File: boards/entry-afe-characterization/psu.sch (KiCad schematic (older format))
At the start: 76 parts, among them J10 CONN_3_PWROUT, Q2 2SA2039-TL-E, U10 LT3042, U11 LT3042, U12 MCP1501T-25E/RW, U13 LT3093, U14 PTN78000AAZ, U15 LT3093, U16 LT3042, U17 TL431ACDBZR, U8 TPS54227-DRC, U9 LT3042

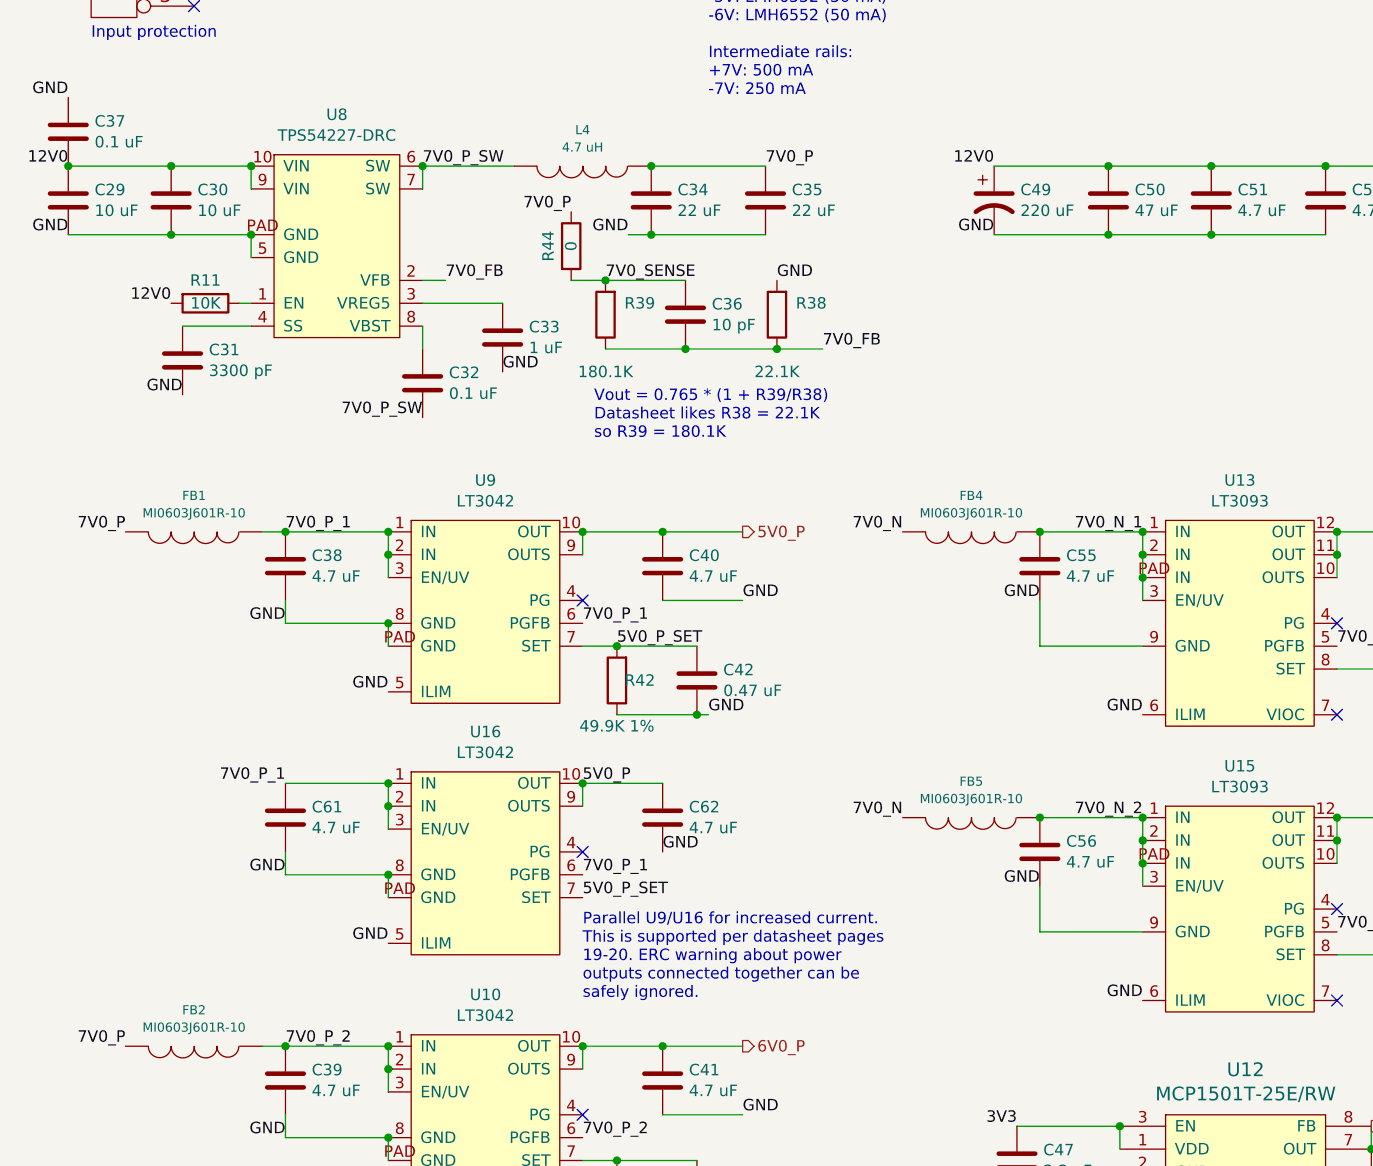
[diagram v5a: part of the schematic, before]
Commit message: Continued design review, added U18 to offset stage
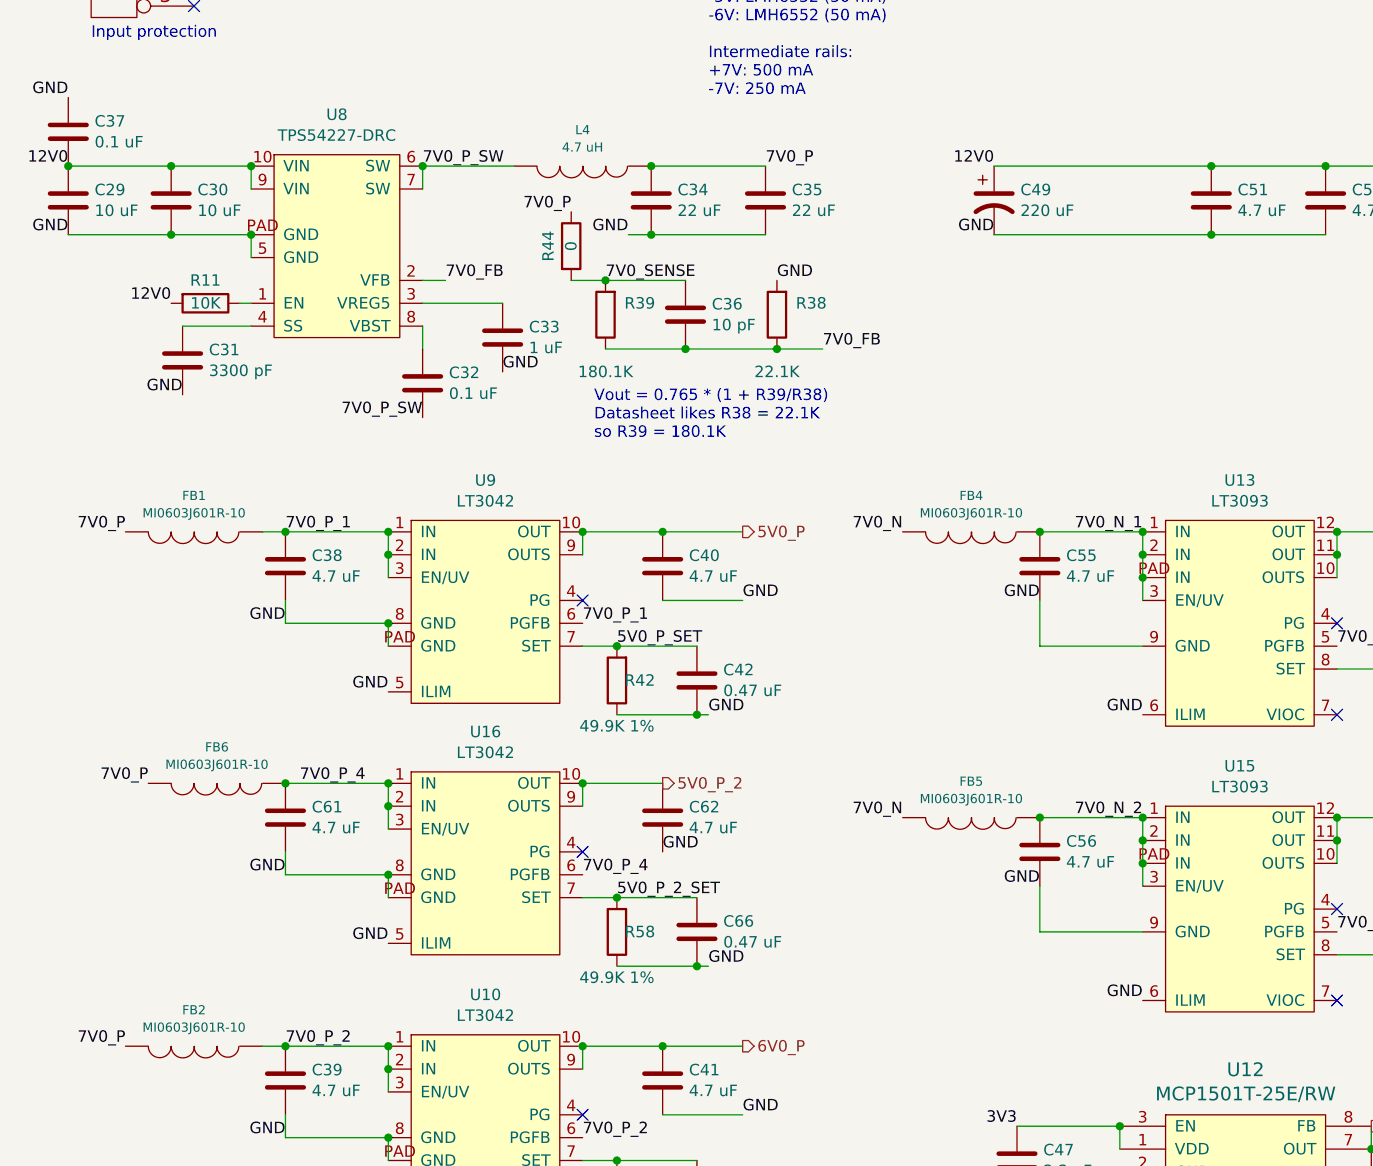
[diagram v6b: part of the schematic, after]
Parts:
- removed C50: 47 uF, symbol device:C
- added C66: 0.47 uF, symbol device:C
- added FB6: MI0603J601R-10, symbol passive-azonenberg:INDUCTOR_PWROUT
- added R58: 49.9K 1%, symbol device:R
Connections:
- net 5V0_P: no longer C62.1, U16.10 (OUT), U16.9 (OUTS)
- net 5V0_P_SET: no longer U16.7 (SET)
- net 7V0_P: now also FB6.2
- net 7V0_P_1: no longer C61.1, U16.1 (IN), U16.2 (IN), U16.3 (EN/UV), U16.6 (PGFB)
- net GND: now also C66.2, R58.1
- new net 5V0_P_2: C62.1, U16.10 (OUT), U16.9 (OUTS)
- new net 5V0_P_2_SET: C66.1, R58.2, U16.7 (SET)
- new net 7V0_P_4: C61.1, FB6.1, U16.1 (IN), U16.2 (IN), U16.3 (EN/UV), U16.6 (PGFB)
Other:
- note removed: "Parallel U9/U16 for increased current.\nThis is supported per datasheet pages\n19-20. ERC warning about power\noutputs connected together can be\nsafely ignored."
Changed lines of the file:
@@
 Sheet 2 8
 Title "Entry-Level Oscilloscope AFE Characterization Platform"
-Date "2020-03-26"
+Date "2020-03-27"
 Rev "0.1"
 Comp "Antikernel Labs"
@@
 Text Label 8200 2000 2    50   ~ 0
 GND
-$Comp
-L device:C C50
-U 1 1 5E865008
-P 5250 1850
-F 0 "C50" H 5365 1896 50  0000 L CNN
-F 1 "47 uF" H 5365 1805 50  0000 L CNN
-F 2 "" H 5288 1700 50  0001 C CNN
-F 3 "" H 5250 1850 50  0001 C CNN
-	1    5250 1850
-	1    0    0    -1
-$EndComp
 Text Label 4750 2000 2    50   ~ 0
 GND
@@
 	1    0    0    -1
 $EndComp
-Wire Wire Line
-	4750 1700 5250 1700
-Wire Wire Line
-	4750 2000 5250 2000
 $Comp
 L device:C C51
@@
 	1    0    0    -1
 $EndComp
-Wire Wire Line
-	5250 1700 5700 1700
-Connection ~ 5250 1700
 Connection ~ 5700 1700
 Wire Wire Line
@@
 Wire Wire Line
 	6200 2000 5700 2000
-Connection ~ 5250 2000
 Connection ~ 5700 2000
-Wire Wire Line
-	5700 2000 5250 2000
 $Comp
 L device:C C55
@@
 Text Label 3100 3800 0    50   ~ 0
 5V0_P_SET
-Text Label 2950 4900 0    50   ~ 0
-5V0_P_SET
-Text Label 2950 4400 0    50   ~ 0
-5V0_P
 Wire Wire Line
 	2950 4500 2950 4400
-Text Label 1650 4400 2    50   ~ 0
-7V0_P_1
+Text Label 2000 4400 2    50   ~ 0
+7V0_P_4
 $Comp
 L device:C C61
@@
 	2100 4500 2100 4600
 Text Label 2950 4800 0    50   ~ 0
-7V0_P_1
+7V0_P_4
 NoConn ~ 2950 4700
 $Comp
@@
 Text Label 3300 4700 0    50   ~ 0
 GND
-Text Notes 2950 5350 0    50   ~ 0
-Parallel U9/U16 for increased current.\nThis is supported per datasheet pages\n19-20. ERC warning about power\noutputs connected together can be\nsafely ignored.
 Text Label 5450 7500 2    50   ~ 0
 5V0_N
@@
 Wire Wire Line
 	1850 800  1950 800
+$Comp
+L device:R R58
+U 1 1 5EA11E7C
+P 3100 5050
+F 0 "R58" H 3000 5050 50  0000 C CNN
+F 1 "49.9K 1%" H 3100 5250 50  0000 C CNN
+F 2 "" V 3030 5050 50  0001 C CNN
+F 3 "" H 3100 5050 50  0001 C CNN
+	1    3100 5050
+	-1   0    0    1
+$EndComp
+Wire Wire Line
+	3100 4900 2950 4900
+Text Label 3500 5200 0    50   ~ 0
+GND
+$Comp
+L device:C C66
+U 1 1 5EA11E88
+P 3450 5050
+F 0 "C66" H 3565 5096 50  0000 L CNN
+F 1 "0.47 uF" H 3565 5005 50  0000 L CNN
+F 2 "" H 3488 4900 50  0001 C CNN
+F 3 "" H 3450 5050 50  0001 C CNN
+	1    3450 5050
+	1    0    0    -1
+$EndComp
+Wire Wire Line
+	3100 5200 3450 5200
+Connection ~ 3450 5200
+Wire Wire Line
+	3450 5200 3500 5200
+Wire Wire Line
+	3450 4900 3100 4900
+Connection ~ 3100 4900
+Text Label 3100 4900 0    50   ~ 0
+5V0_P_2_SET
+Text HLabel 3300 4400 2    50   Output ~ 0
+5V0_P_2
+Text Label 1050 4400 2    50   ~ 0
+7V0_P
+$Comp
+L passive-azonenberg:INDUCTOR_PWROUT FB6
+U 1 1 5EA19602
+P 1350 4400
+F 0 "FB6" V 1192 4400 40  0000 C CNN
+F 1 "MI0603J601R-10" V 1268 4400 40  0000 C CNN
+F 2 "" H 1350 4400 60  0000 C CNN
+F 3 "" H 1350 4400 60  0000 C CNN
+	1    1350 4400
+	0    1    1    0
+$EndComp
+Connection ~ 1650 4400
+Wire Wire Line
+	4750 1700 5700 1700
+Wire Wire Line
+	4750 2000 5700 2000
 $EndSCHEMATC

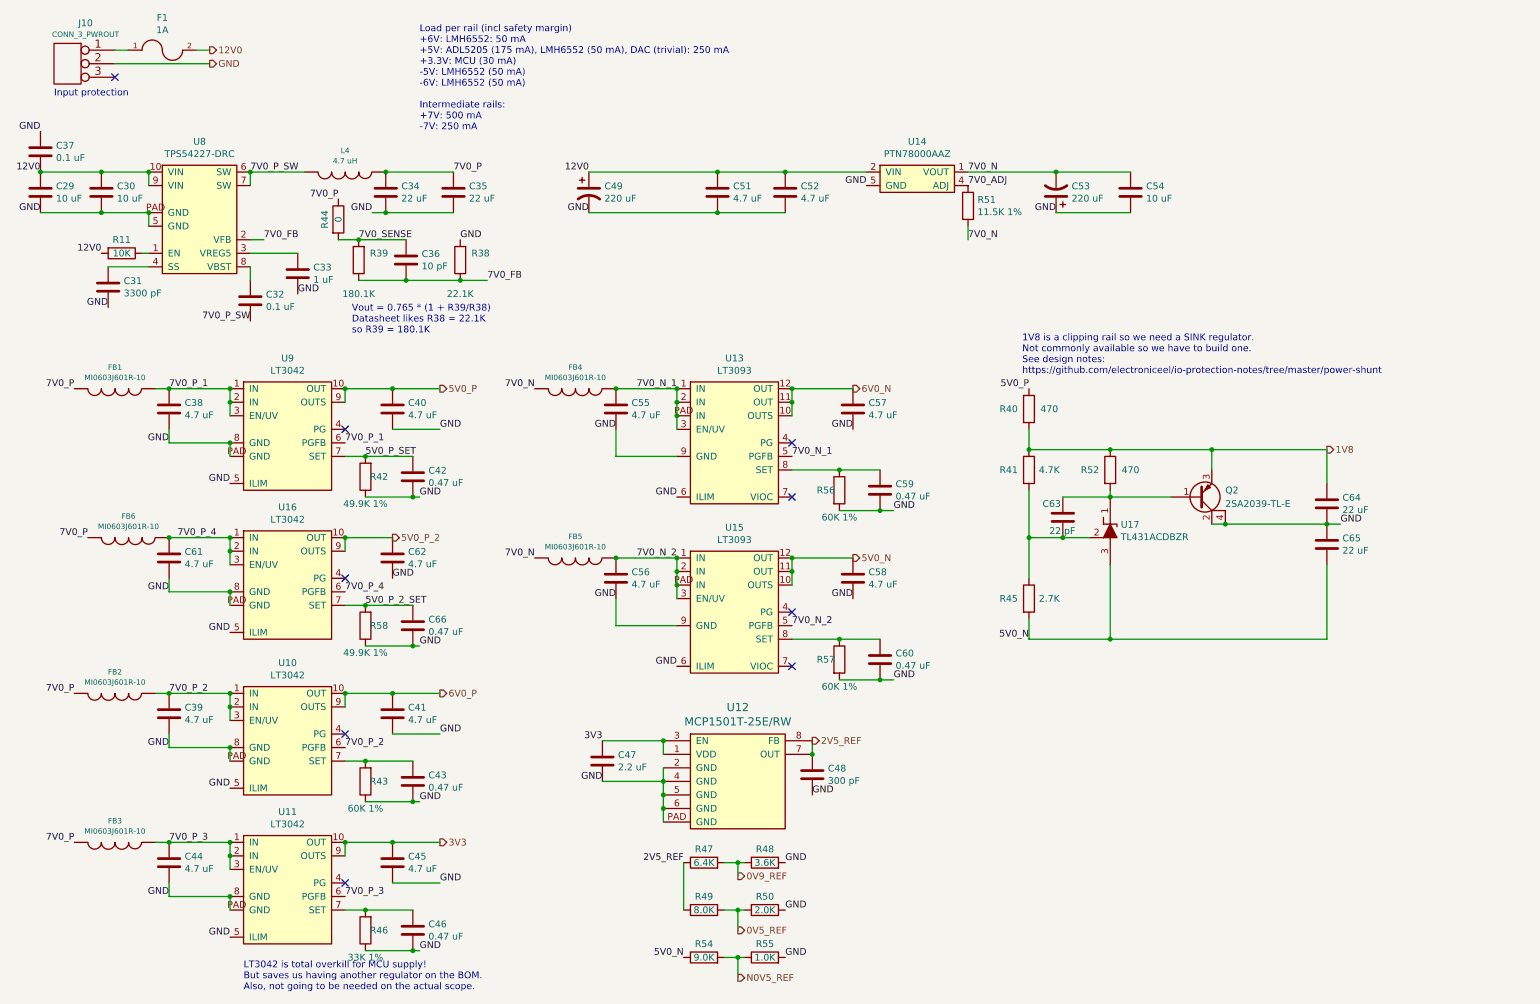
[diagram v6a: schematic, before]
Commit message: Continued design review, began assigning footprints to sch symbols
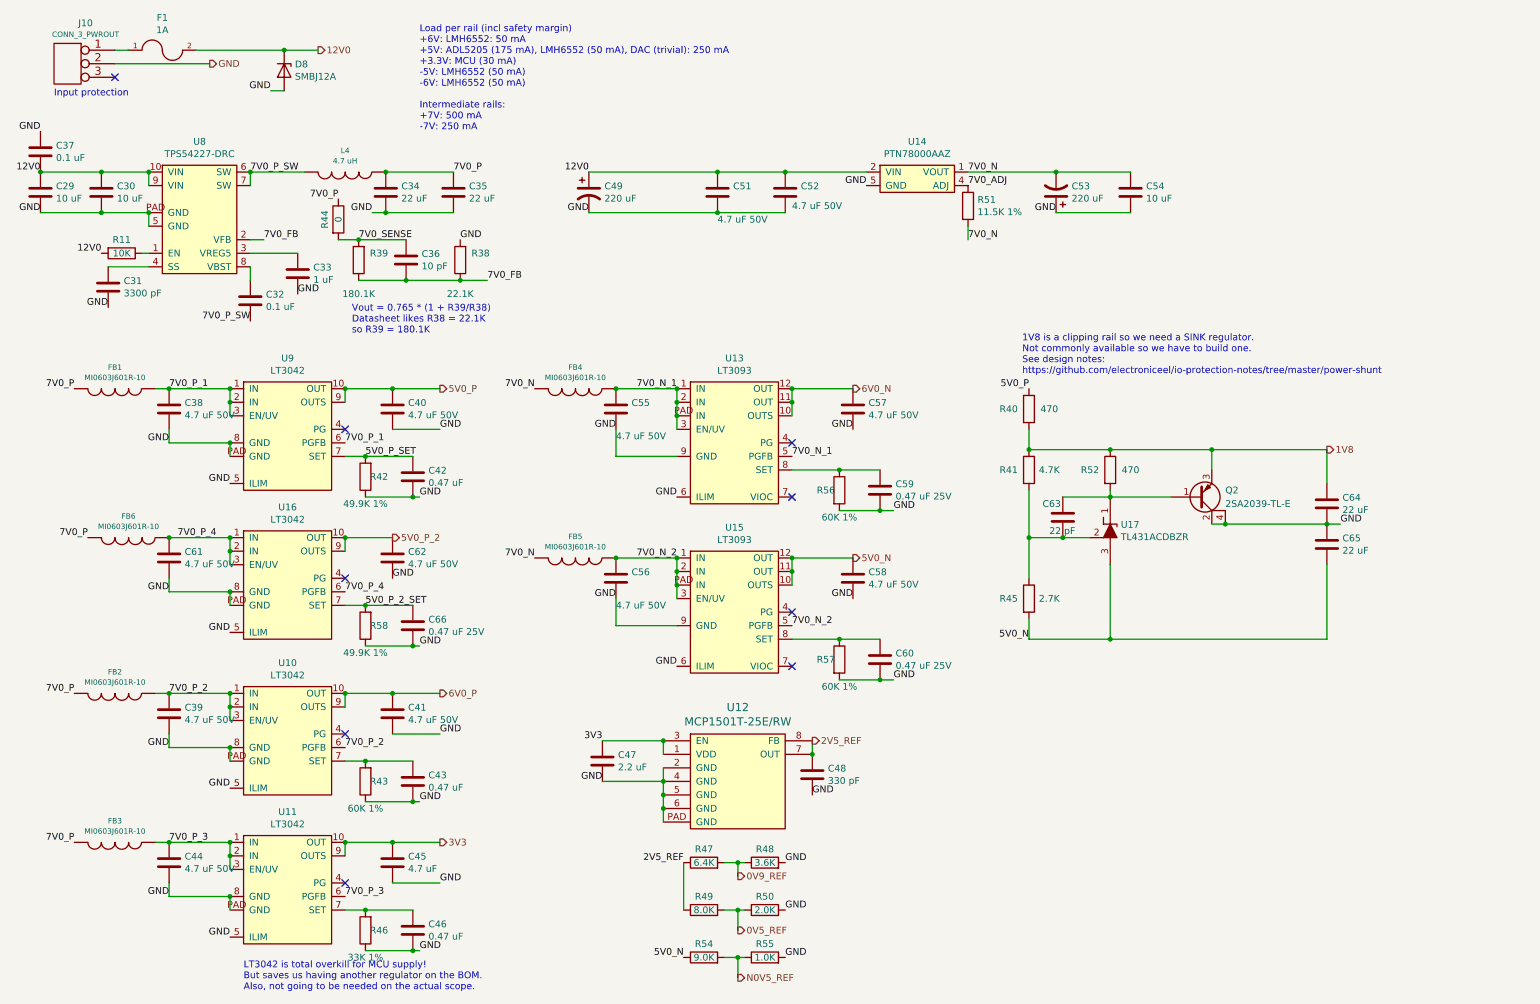
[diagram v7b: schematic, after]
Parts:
- added D8: SMBJ12A, azonenberg_pcb:SMB, symbol device:D_Zener
- C29, C30, C34, C35, C54: footprint (none) -> azonenberg_pcb:EIA_1210_CAP_NOSILK
- C31, C33, C45, C47: footprint (none) -> azonenberg_pcb:EIA_0603_CAP_NOSILK
- C32, C36, C37, C42, C43, C46, C63: footprint (none) -> azonenberg_pcb:EIA_0402_CAP_NOSILK
- C38, C39, C40, C41, C44, C51, C52, C55, C56, C57, C58, C61, C62: value 4.7 uF -> 4.7 uF 50V; footprint (none) -> azonenberg_pcb:EIA_0805_CAP_NOSILK
- C48: value 300 pF -> 330 pF; footprint (none) -> azonenberg_pcb:EIA_0603_CAP_NOSILK
- C49, C53: footprint (none) -> azonenberg_pcb:CAP_AL_6.3MM_SMT
- C59, C60, C66: value 0.47 uF -> 0.47 uF 25V; footprint (none) -> azonenberg_pcb:EIA_0402_CAP_NOSILK
- C64, C65: footprint (none) -> azonenberg_pcb:EIA_0805_CAP_NOSILK
- F1: footprint (none) -> azonenberg_pcb:EIA_0402_RES_NOSILK
- FB1, FB2, FB3, FB4, FB5, FB6: footprint (none) -> azonenberg_pcb:EIA_0603_INDUCTOR_NOSILK
- J10: footprint (none) -> azonenberg_pcb:CONN_CUI_PJ-058BH_HIPWR_BARREL_NOSLOT
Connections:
- net 12V0: now also D8.1 (K)
- net GND: now also D8.2 (A)
